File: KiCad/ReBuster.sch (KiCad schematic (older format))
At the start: 10 parts, among them U3 SN74CBTD16210, U4 SN74CBTD16210, U5 SN74CBTD16210, U6 SN74CBTD16210, U7 PLCC_84_plug, U8 PLCC_84_plug

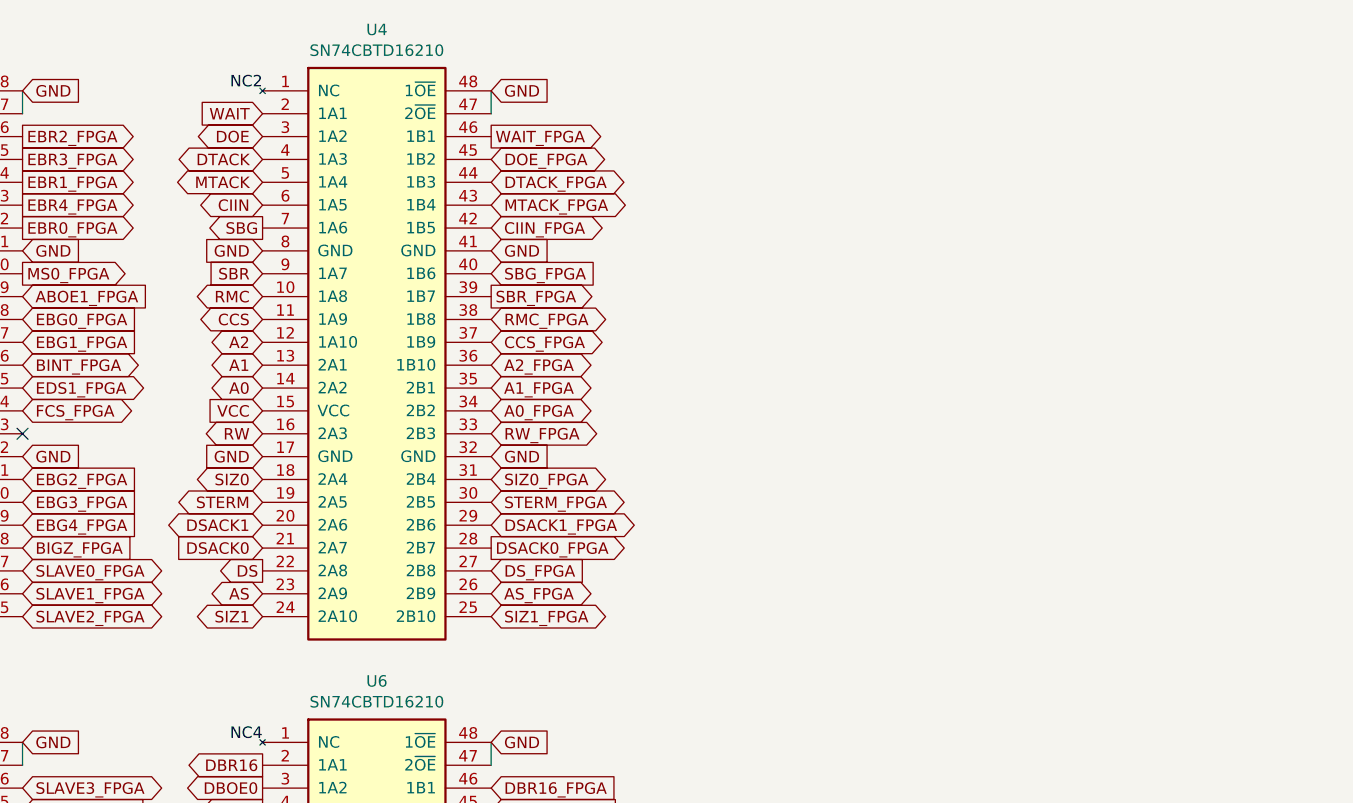
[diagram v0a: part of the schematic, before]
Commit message: replace U4 (SN74CBTD16210) with a SN74LVC16T245DGVR
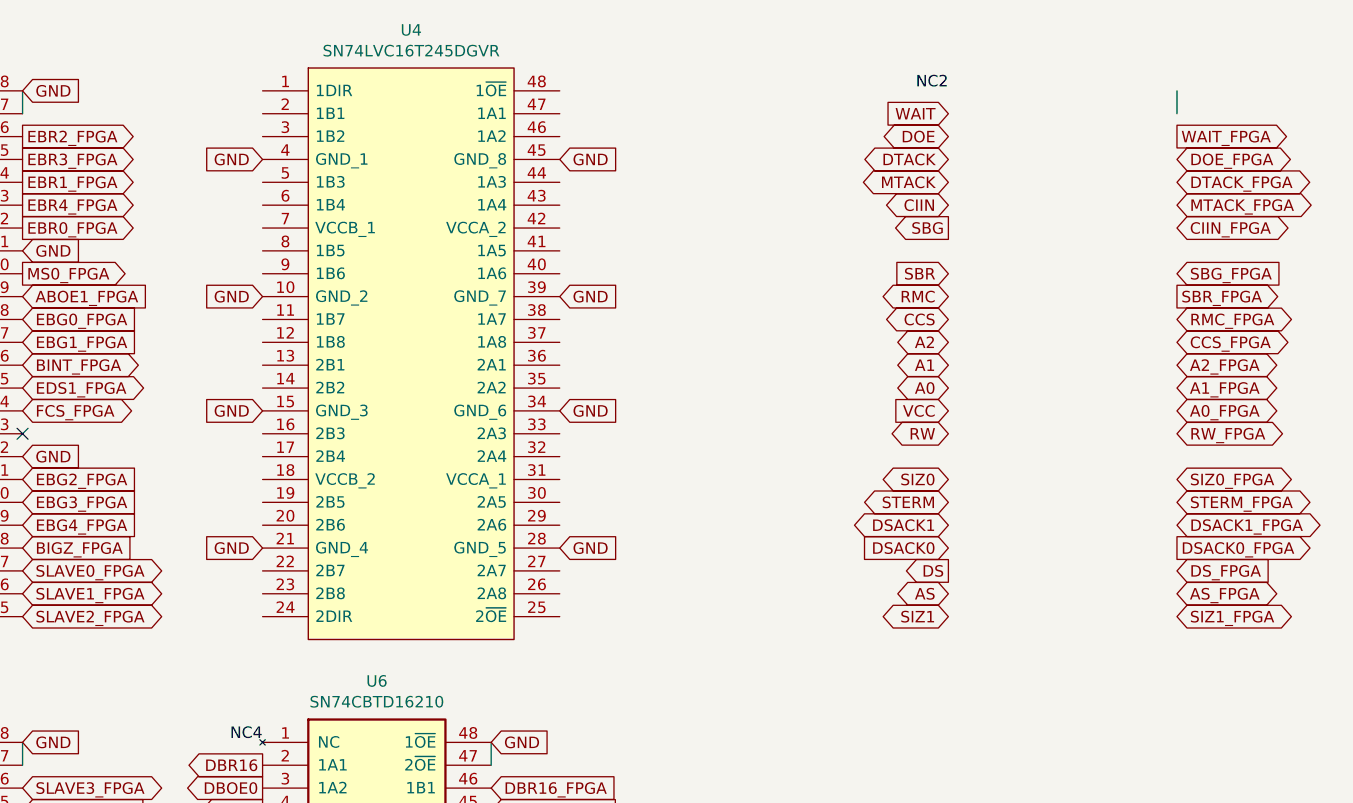
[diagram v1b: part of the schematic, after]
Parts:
- removed U4: SN74CBTD16210, ReBuster:TSSOP-48_6.1x12.5mm_P0.5mm_padLength_1mm, symbol ReBuster:SN74CBTD16210
- added U4: SN74LVC16T245DGVR, Package_SO:TSSOP-48_4.4x9.7mm_P0.4mm, symbol ReBuster:SN74LVC16T245DGVR
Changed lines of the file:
@@
 FCS
-$Comp
-L ReBuster:SN74CBTD16210 U4
-U 1 1 605AF950
-P 9700 2050
-F 0 "U4" H 9700 3417 50  0000 C CNN
-F 1 "SN74CBTD16210" H 9700 3326 50  0000 C CNN
-F 2 "ReBuster:TSSOP-48_6.1x12.5mm_P0.5mm_padLength_1mm" H 11350 2500 50  0001 C CNN
-F 3 "https://www.ti.com/lit/ds/symlink/sn74cbtd16210.pdf" H 11350 2500 50  0001 C CNN
-	1    9700 2050
-	1    0    0    -1
-$EndComp
 $Comp
 L ReBuster:SN74CBTD16210 U5
@@
 	1    0    0    -1
 $EndComp
-Text Label 9200 950  2    50   ~ 0
+Text Label 12200 950  2    50   ~ 0
 NC2
 Text Label 7150 3800 2    50   ~ 0
@@
 Connection ~ 2850 7150
 Wire Wire Line
-	10200 1050 10200 950
+	13200 1050 13200 950
 Wire Wire Line
 	10200 3900 10200 3800
@@
 Text GLabel 8150 1650 2    50   Input ~ 0
 GND
-Text GLabel 10200 2550 2    50   Input ~ 0
-GND
-Text GLabel 10200 950  2    50   Input ~ 0
-GND
-Text GLabel 10200 1650 2    50   Input ~ 0
+Text GLabel 10500 1850 2    50   Input ~ 0
+GND
+Text GLabel 9200 1250 0    50   Input ~ 0
+GND
+Text GLabel 10500 1250 2    50   Input ~ 0
 GND
 Text GLabel 10200 5400 2    50   Input ~ 0
@@
 Text GLabel 8150 4500 2    50   Input ~ 0
 GND
+Text GLabel 12200 2350 0    50   Input ~ 0
+VCC
+Text GLabel 9200 1850 0    50   Input ~ 0
+GND
 Text GLabel 9200 2350 0    50   Input ~ 0
-VCC
-Text GLabel 9200 1650 0    50   Input ~ 0
-GND
-Text GLabel 9200 2550 0    50   Input ~ 0
 GND
 Text GLabel 9200 5200 0    50   Input ~ 0
@@
 Text GLabel 7150 5200 0    50   Input ~ 0
 VCC
-Text GLabel 10200 3250 2    50   BiDi ~ 0
+Text GLabel 13200 3250 2    50   BiDi ~ 0
 SIZ1_FPGA
 Text GLabel 8150 1450 2    50   Output ~ 0
@@
 Text GLabel 8150 3250 2    50   BiDi ~ 0
 SLAVE2_FPGA
-Text GLabel 10200 1150 2    50   Output ~ 0
+Text GLabel 13200 1150 2    50   Output ~ 0
 WAIT_FPGA
-Text GLabel 10200 1250 2    50   BiDi ~ 0
+Text GLabel 13200 1250 2    50   BiDi ~ 0
 DOE_FPGA
-Text GLabel 10200 1350 2    50   BiDi ~ 0
+Text GLabel 13200 1350 2    50   BiDi ~ 0
 DTACK_FPGA
-Text GLabel 10200 1450 2    50   BiDi ~ 0
+Text GLabel 13200 1450 2    50   BiDi ~ 0
 MTACK_FPGA
-Text GLabel 10200 1550 2    50   BiDi ~ 0
+Text GLabel 13200 1550 2    50   BiDi ~ 0
 CIIN_FPGA
-Text GLabel 10200 1850 2    50   Output ~ 0
+Text GLabel 13200 1850 2    50   Output ~ 0
 SBR_FPGA
-Text GLabel 10200 1950 2    50   BiDi ~ 0
+Text GLabel 13200 1950 2    50   BiDi ~ 0
 RMC_FPGA
-Text GLabel 10200 2050 2    50   BiDi ~ 0
+Text GLabel 13200 2050 2    50   BiDi ~ 0
 CCS_FPGA
-Text GLabel 10200 2150 2    50   BiDi ~ 0
+Text GLabel 13200 2150 2    50   BiDi ~ 0
 A2_FPGA
-Text GLabel 10200 2250 2    50   BiDi ~ 0
+Text GLabel 13200 2250 2    50   BiDi ~ 0
 A1_FPGA
-Text GLabel 10200 1750 2    50   Input ~ 0
+Text GLabel 13200 1750 2    50   Input ~ 0
 SBG_FPGA
-Text GLabel 10200 2450 2    50   BiDi ~ 0
+Text GLabel 13200 2450 2    50   BiDi ~ 0
 RW_FPGA
-Text GLabel 10200 2650 2    50   BiDi ~ 0
+Text GLabel 13200 2650 2    50   BiDi ~ 0
 SIZ0_FPGA
-Text GLabel 10200 2750 2    50   BiDi ~ 0
+Text GLabel 13200 2750 2    50   BiDi ~ 0
 STERM_FPGA
-Text GLabel 10200 3050 2    50   Input ~ 0
+Text GLabel 13200 3050 2    50   Input ~ 0
 DS_FPGA
-Text GLabel 10200 3150 2    50   BiDi ~ 0
+Text GLabel 13200 3150 2    50   BiDi ~ 0
 AS_FPGA
 Text GLabel 8150 4000 2    50   BiDi ~ 0
@@
 Text GLabel 7150 2250 0    50   BiDi ~ 0
 FCS
-Text GLabel 9200 1950 0    50   BiDi ~ 0
+Text GLabel 12200 1950 0    50   BiDi ~ 0
 CCS
-Text GLabel 9200 2050 0    50   BiDi ~ 0
+Text GLabel 12200 2050 0    50   BiDi ~ 0
 A2
-Text GLabel 9200 2150 0    50   BiDi ~ 0
+Text GLabel 12200 2150 0    50   BiDi ~ 0
 A1
-Text GLabel 9200 2250 0    50   BiDi ~ 0
+Text GLabel 12200 2250 0    50   BiDi ~ 0
 A0
-Text GLabel 9200 2450 0    50   BiDi ~ 0
+Text GLabel 12200 2450 0    50   BiDi ~ 0
 RW
-Text GLabel 9200 2650 0    50   BiDi ~ 0
+Text GLabel 12200 2650 0    50   BiDi ~ 0
 SIZ0
-Text GLabel 9200 3250 0    50   BiDi ~ 0
+Text GLabel 12200 3250 0    50   BiDi ~ 0
 SIZ1
-Text GLabel 9200 3150 0    50   BiDi ~ 0
+Text GLabel 12200 3150 0    50   BiDi ~ 0
 AS
-Text GLabel 9200 3050 0    50   Output ~ 0
+Text GLabel 12200 3050 0    50   Output ~ 0
 DS
-Text GLabel 9200 2950 0    50   Input ~ 0
+Text GLabel 12200 2950 0    50   Input ~ 0
 DSACK0
-Text GLabel 9200 2850 0    50   BiDi ~ 0
+Text GLabel 12200 2850 0    50   BiDi ~ 0
 DSACK1
-Text GLabel 9200 2750 0    50   BiDi ~ 0
+Text GLabel 12200 2750 0    50   BiDi ~ 0
 STERM
 Wire Wire Line
@@
 Wire Wire Line
 	2750 5900 2750 6000
-Text GLabel 9200 1850 0    50   BiDi ~ 0
+Text GLabel 12200 1850 0    50   BiDi ~ 0
 RMC
-Text GLabel 9200 1750 0    50   Input ~ 0
+Text GLabel 12200 1750 0    50   Input ~ 0
 SBR
-Text GLabel 9200 1550 0    50   Output ~ 0
+Text GLabel 12200 1550 0    50   Output ~ 0
 SBG
-Text GLabel 9200 1450 0    50   BiDi ~ 0
+Text GLabel 12200 1450 0    50   BiDi ~ 0
 CIIN
 Wire Wire Line
 	2750 5350 2750 5450
-Text GLabel 9200 1350 0    50   BiDi ~ 0
+Text GLabel 12200 1350 0    50   BiDi ~ 0
 MTACK
-Text GLabel 9200 1250 0    50   BiDi ~ 0
+Text GLabel 12200 1250 0    50   BiDi ~ 0
 DTACK
-Text GLabel 9200 1150 0    50   BiDi ~ 0
+Text GLabel 12200 1150 0    50   BiDi ~ 0
 DOE
-Text GLabel 9200 1050 0    50   Input ~ 0
+Text GLabel 12200 1050 0    50   Input ~ 0
 WAIT
 Text GLabel 9200 6100 0    50   BiDi ~ 0
@@
 EBR0_FPGA
 NoConn ~ 8150 2450
-Text GLabel 10200 2350 2    50   BiDi ~ 0
+Text GLabel 13200 2350 2    50   BiDi ~ 0
 A0_FPGA
-Text GLabel 10200 2850 2    50   BiDi ~ 0
+Text GLabel 13200 2850 2    50   BiDi ~ 0
 DSACK1_FPGA
-Text GLabel 10200 2950 2    50   Output ~ 0
+Text GLabel 13200 2950 2    50   Output ~ 0
 DSACK0_FPGA
 NoConn ~ 10200 5200
+$Comp
+L ReBuster:SN74LVC16T245DGVR U4
+U 1 1 69A5D76D
+P 9850 2100
+F 0 "U4" H 9850 3515 50  0000 C CNN
+F 1 "SN74LVC16T245DGVR" H 9850 3424 50  0000 C CNN
+F 2 "Package_SO:TSSOP-48_4.4x9.7mm_P0.4mm" H 10350 3350 50  0001 L CNN
+F 3 "http://www.ti.com/lit/gpn/sn74lvc16t245" H 10350 3250 50  0001 L CNN
+	1    9850 2100
+	1    0    0    -1
+$EndComp
+Text GLabel 10500 2350 2    50   Input ~ 0
+GND
+Text GLabel 10500 2950 2    50   Input ~ 0
+GND
+Text GLabel 9200 2950 0    50   Input ~ 0
+GND
 $EndSCHEMATC

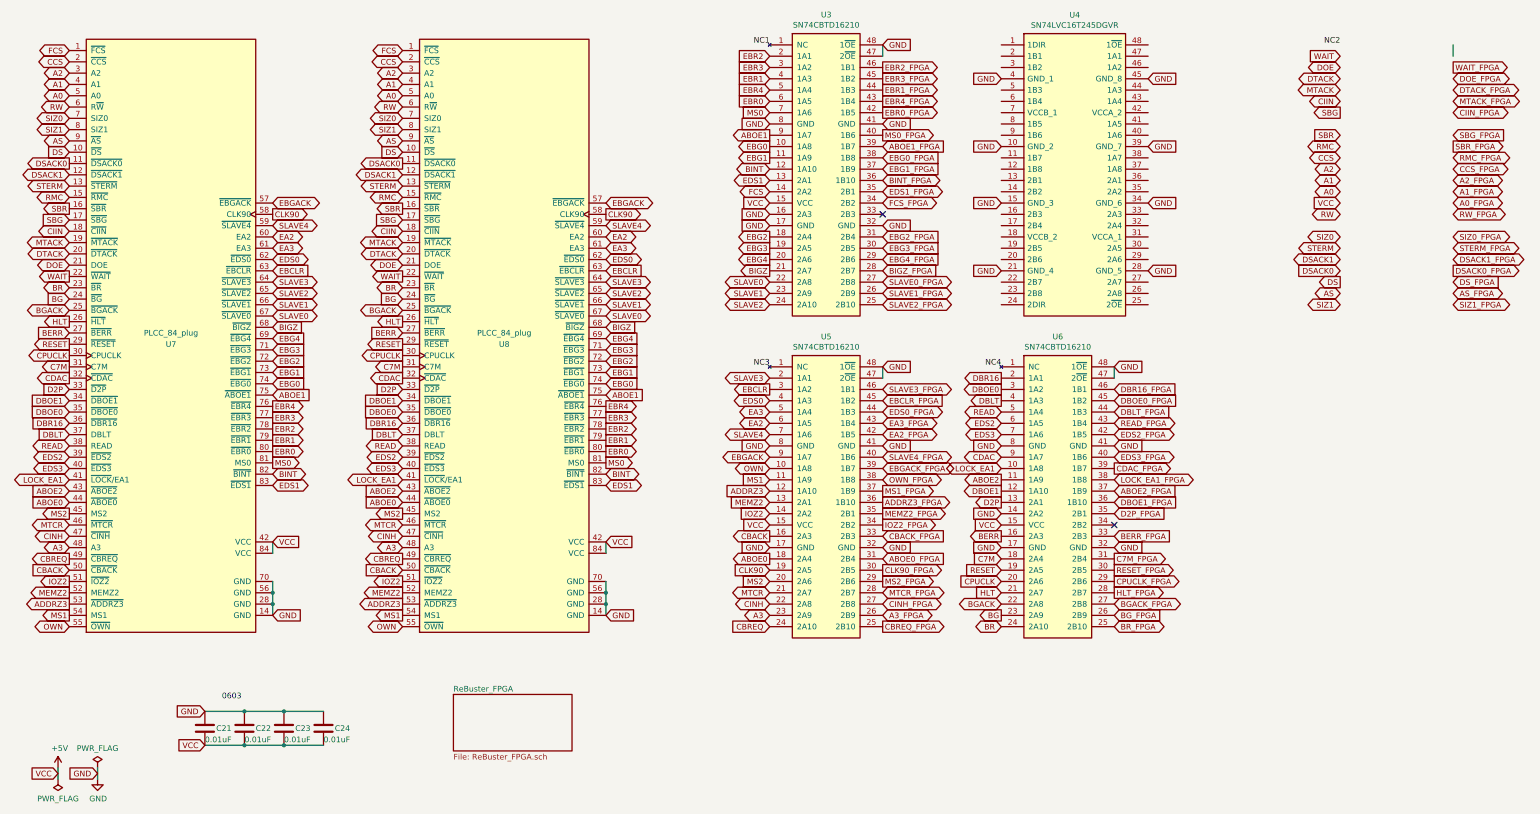
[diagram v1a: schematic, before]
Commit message: Add 74LVC2T45DC for handling DTACKn and MTACKn
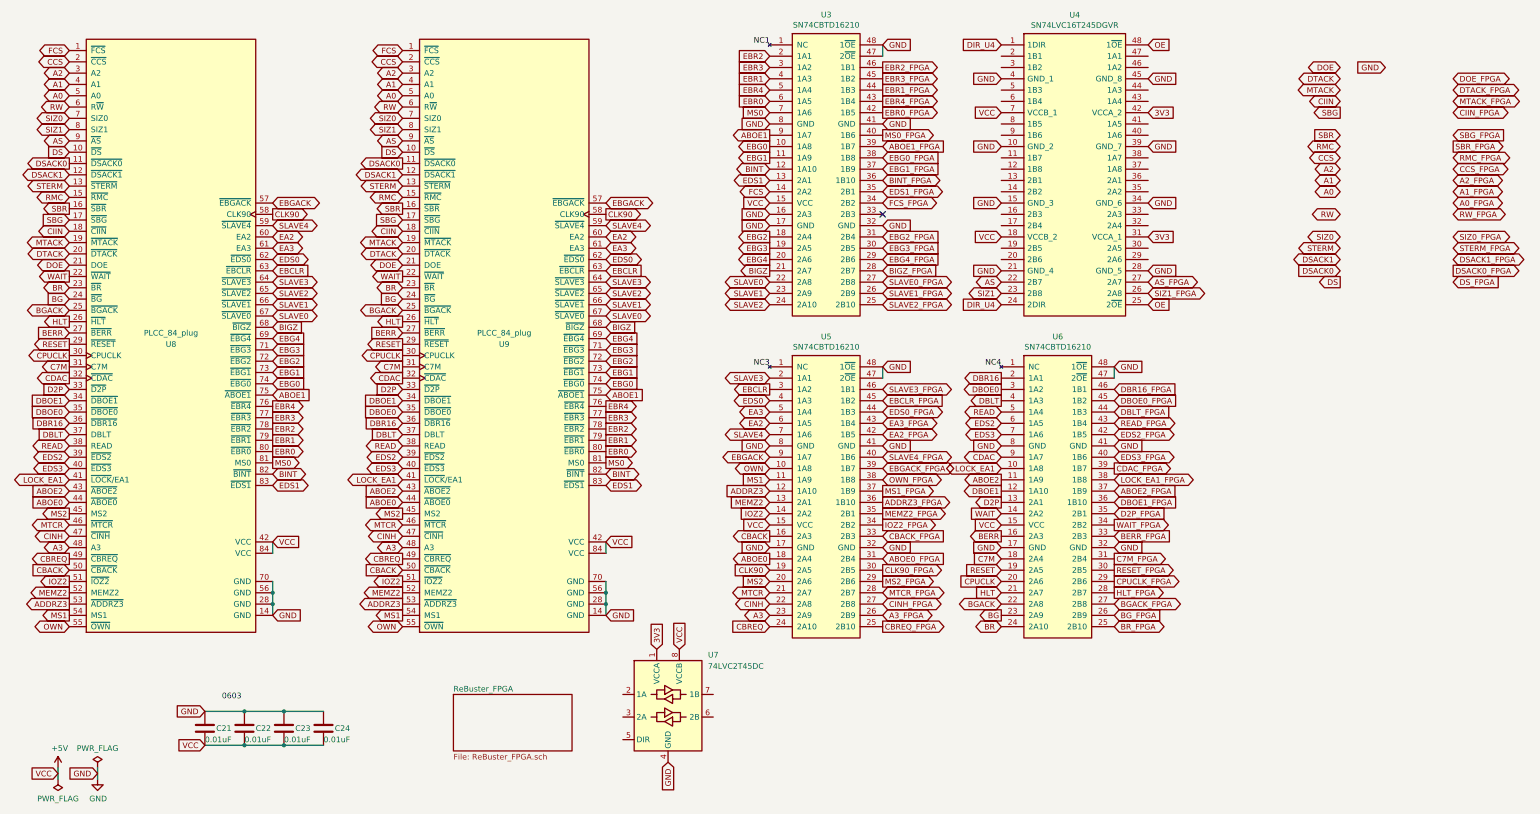
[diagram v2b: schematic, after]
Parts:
- added U7: 74LVC2T45DC, Package_SO:VSSOP-8_2.3x2mm_P0.5mm, symbol Logic_LevelTranslator:74LVC2T45DC
- renumbered U7 to U8, U8 to U9
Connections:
- net labels added: 3V3, DIR_U4, OE
- net labels removed: NC2
- wire segments 20 -> 19
- no-connect marks 2 -> 1
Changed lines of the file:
@@
 	1    0    0    -1
 $EndComp
-Text Label 12200 950  2    50   ~ 0
-NC2
 Text Label 7150 3800 2    50   ~ 0
 NC3
@@
 Connection ~ 2850 6850
 Connection ~ 2850 7150
-Wire Wire Line
-	13200 1050 13200 950
 Wire Wire Line
 	10200 3900 10200 3800
@@
 Text GLabel 8150 4500 2    50   Input ~ 0
 GND
-Text GLabel 12200 2350 0    50   Input ~ 0
+Text GLabel 9200 1550 0    50   Input ~ 0
 VCC
 Text GLabel 9200 1850 0    50   Input ~ 0
@@
 Text GLabel 7150 5200 0    50   Input ~ 0
 VCC
-Text GLabel 13200 3250 2    50   BiDi ~ 0
+Text GLabel 10500 3150 2    50   BiDi ~ 0
 SIZ1_FPGA
 Text GLabel 8150 1450 2    50   Output ~ 0
@@
 Text GLabel 8150 3250 2    50   BiDi ~ 0
 SLAVE2_FPGA
-Text GLabel 13200 1150 2    50   Output ~ 0
+Text GLabel 10200 5200 2    50   Output ~ 0
 WAIT_FPGA
 Text GLabel 13200 1250 2    50   BiDi ~ 0
@@
 Text GLabel 13200 3050 2    50   Input ~ 0
 DS_FPGA
-Text GLabel 13200 3150 2    50   BiDi ~ 0
+Text GLabel 10500 3050 2    50   BiDi ~ 0
 AS_FPGA
 Text GLabel 8150 4000 2    50   BiDi ~ 0
@@
 $EndComp
 $Comp
-L ReBuster:Super_Buster_socket U7
+L ReBuster:Super_Buster_socket U8
 U 1 1 65330DEC
 P 1850 3500
-F 0 "U7" H 1850 3400 50  0000 C CNN
+F 0 "U8" H 1850 3400 50  0000 C CNN
 F 1 "PLCC_84_plug" H 1850 3500 50  0000 C CNN
 F 2 "ReBuster:PLCC-84_Plug_P1.27mm_mirrored" H 2250 6000 50  0001 L CIN
@@
 Text GLabel 12200 2650 0    50   BiDi ~ 0
 SIZ0
-Text GLabel 12200 3250 0    50   BiDi ~ 0
+Text GLabel 9200 3150 0    50   BiDi ~ 0
 SIZ1
-Text GLabel 12200 3150 0    50   BiDi ~ 0
+Text GLabel 9200 3050 0    50   BiDi ~ 0
 AS
 Text GLabel 12200 3050 0    50   Output ~ 0
@@
 Text GLabel 12200 1150 0    50   BiDi ~ 0
 DOE
-Text GLabel 12200 1050 0    50   Input ~ 0
+Text GLabel 9200 5100 0    50   Input ~ 0
 WAIT
 Text GLabel 9200 6100 0    50   BiDi ~ 0
@@
 EDS0
 $Comp
-L ReBuster:Super_Buster_socket U8
+L ReBuster:Super_Buster_socket U9
 U 1 1 67490817
 P 4800 3500
-F 0 "U8" H 4800 3400 50  0000 C CNN
+F 0 "U9" H 4800 3400 50  0000 C CNN
 F 1 "PLCC_84_plug" H 4800 3500 50  0000 C CNN
 F 2 "ReBuster:PLCC-84_TH_pin_holes" H 5200 6000 50  0001 L CIN
@@
 Wire Wire Line
 	5700 5900 5700 6000
-Text GLabel 9200 5100 0    50   Input ~ 0
+Text GLabel 12600 1150 0    50   Input ~ 0
 GND
 Text GLabel 7150 2450 0    50   Input ~ 0
@@
 Text GLabel 13200 2950 2    50   Output ~ 0
 DSACK0_FPGA
-NoConn ~ 10200 5200
 $Comp
 L ReBuster:SN74LVC16T245DGVR U4
@@
 Text GLabel 9200 2950 0    50   Input ~ 0
 GND
+Text GLabel 9200 950  0    50   Input ~ 0
+DIR_U4
+Text GLabel 9200 3250 0    50   Input ~ 0
+DIR_U4
+Text GLabel 10500 950  2    50   Input ~ 0
+OE
+Text GLabel 10500 3250 2    50   Input ~ 0
+OE
+Text GLabel 9200 2650 0    50   Input ~ 0
+VCC
+Text GLabel 10500 1550 2    50   Input ~ 0
+3V3
+Text GLabel 10500 2650 2    50   Input ~ 0
+3V3
+$Comp
+L Logic_LevelTranslator:74LVC2T45DC U7
+U 1 1 69AF9BA6
+P 6250 6800
+F 0 "U7" H 6650 7250 50  0000 C CNN
+F 1 "74LVC2T45DC" H 6850 7150 50  0000 C CNN
+F 2 "Package_SO:VSSOP-8_2.3x2mm_P0.5mm" H 6250 5950 50  0001 C CNN
+F 3 "https://assets.nexperia.com/documents/data-sheet/74LVC_LVCH2T45.pdf" H 6500 6550 50  0001 C CNN
+	1    6250 6800
+	1    0    0    -1
+$EndComp
+Text GLabel 6150 6300 1    50   Input ~ 0
+3V3
+Text GLabel 6350 6300 1    50   Input ~ 0
+VCC
+Text GLabel 6250 7300 3    50   Input ~ 0
+GND
 $EndSCHEMATC
